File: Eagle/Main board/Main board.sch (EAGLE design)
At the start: 105 parts, among them IC1 LMZ14202TZE-ADJ_NOPB, IC2 VNH7070ASTR, IC3 VNH7070ASTR, IC4 VNH7070ASTR, IC5 VNH7070ASTR, J2 10104111-0001LF, J3 43650-0201, J4 43650-0201, J5 43650-0201, J6 43650-0201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

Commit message: Added every component in BoM
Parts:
- added C25: 100n, rcl:C-EUC0805
- C1: value 1500u -> 100n
- C11, C12, C9: value (none) -> 100u
- C3: value 10n -> 22n
- C7: value (none) -> 1OOu
- RB1, RB2, RB3, RB4: value 33 -> 22
- renumbered CX to C24, SW1L1 to L1, SW2L1 to L2, SW2L2 to L3
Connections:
- net +3V3: now also C25.1
- net GND: now also C25.2
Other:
- moved on the sheet: C15, J1, J3, J4, J5, J6, J_SPI, LS_EST, LS_NORD, LS_OVEST, LS_SUD, R13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

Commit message: BoM finished
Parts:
- renumbered U$3 to IC6

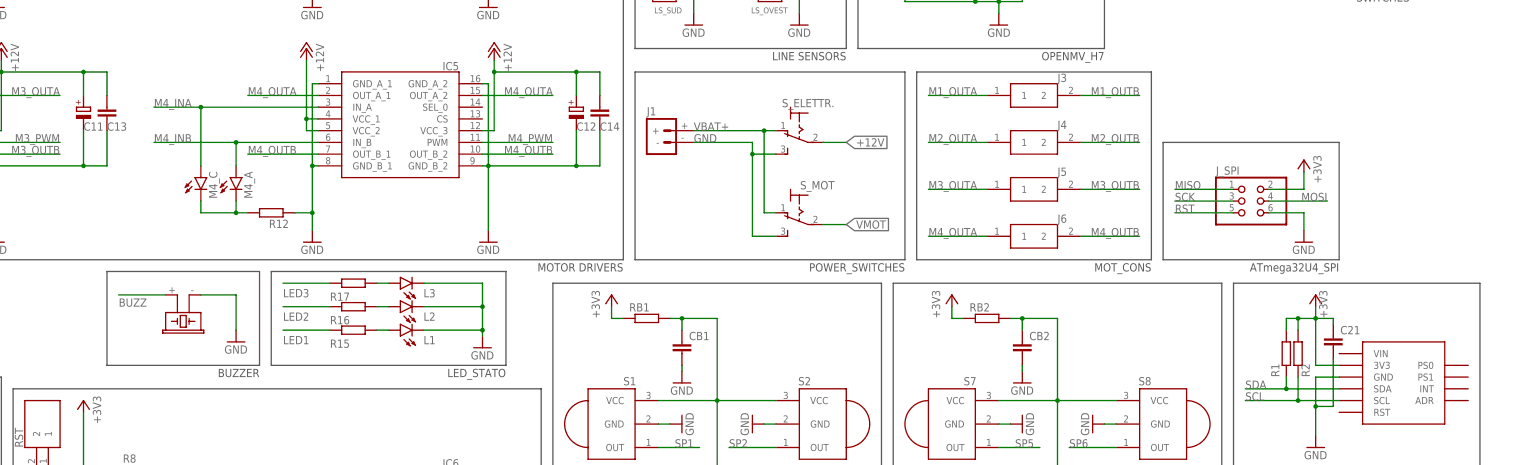
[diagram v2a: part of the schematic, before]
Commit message: Supply planes for motor drivers done
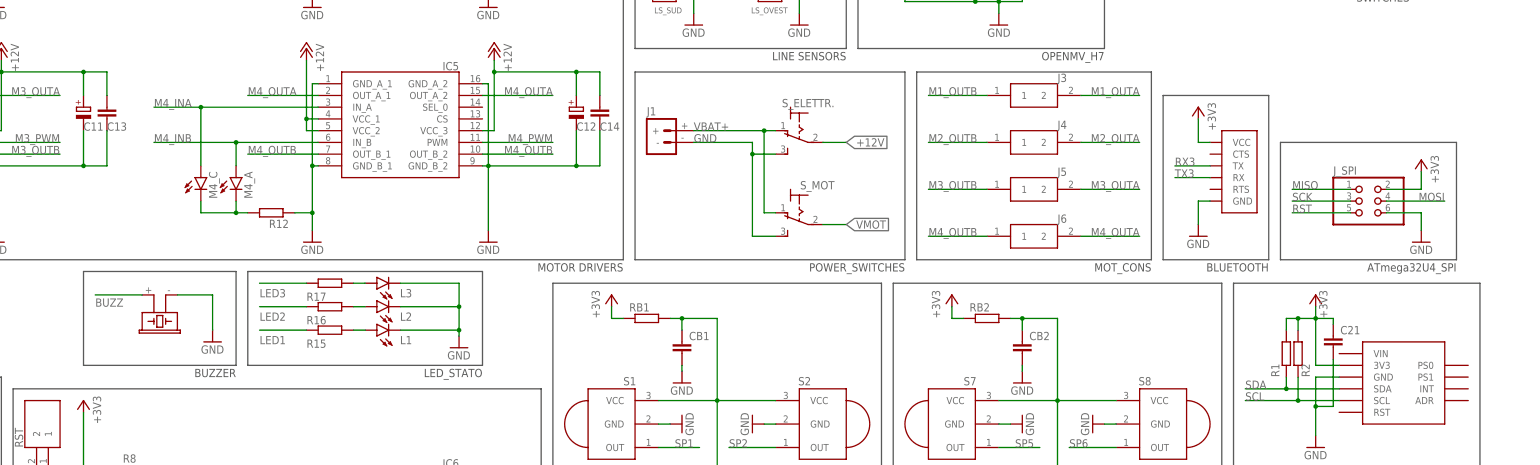
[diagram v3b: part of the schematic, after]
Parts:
- added U$3: BLUESMIRF, BlueSMIRF Silver:BLUESMIRF
- C19, C25, C6: device rcl:C-EUC0805 -> rcl:C-EUC1206
- CB1, CB2, CB3, CB4: device rcl:C-EUC1206 -> rcl:C-EUC0805
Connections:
- net +3V3: now also U$3.VCC
- net GND: now also U$3.GND
- net M1_OUTA: now also J3.2; no longer J3.1
- net M1_OUTB: now also J3.1; no longer J3.2
- net M2_OUTA: now also J4.2; no longer J4.1
- net M2_OUTB: now also J4.1; no longer J4.2
- net M3_OUTA: now also J5.2; no longer J5.1
- net M3_OUTB: now also J5.1; no longer J5.2
- net M4_OUTA: now also J6.2; no longer J6.1
- net M4_OUTB: now also J6.1; no longer J6.2
- net RX3: now also U$3.TX
- net TX3: now also U$3.RX
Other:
- note added: "BLUETOOTH"
- moved on the sheet: J_SPI, L1, L2, L3, R15, R16, R17
